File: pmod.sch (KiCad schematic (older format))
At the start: 13 parts, among them J6 PMOD, U10 AP7381-33SA, U11 TXS0108EPW

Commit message: finished routing, drc passed
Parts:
- U10: symbol Regulator_Linear:AP7381-33SA -> THS-80-rescue:AP7381-33SA-Regulator_Linear
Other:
- moved on the sheet: C14, C15
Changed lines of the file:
@@
 L power:VCC #PWR?
 U 1 1 5DC93B40
-P 2900 1875
+P 2850 2175
 AR Path="/5D70CA34/5DC93B40" Ref="#PWR?"  Part="1"
 AR Path="/5D70CA34/5DC790D1/5DC93B40" Ref="#PWR033"  Part="1"
-F 0 "#PWR033" H 2900 1725 50  0001 C CNN
-F 1 "VCC" H 2917 2048 50  0000 C CNN
-F 2 "" H 2900 1875 50  0001 C CNN
-F 3 "" H 2900 1875 50  0001 C CNN
-	1    2900 1875
+F 0 "#PWR033" H 2850 2025 50  0001 C CNN
+F 1 "VCC" H 2867 2348 50  0000 C CNN
+F 2 "" H 2850 2175 50  0001 C CNN
+F 3 "" H 2850 2175 50  0001 C CNN
+	1    2850 2175
 	1    0    0    -1
 $EndComp
@@
 L power:+3V3 #PWR?
 U 1 1 5DC93B46
-P 4350 1875
+P 4300 2175
 AR Path="/5D70CA34/5DC93B46" Ref="#PWR?"  Part="1"
 AR Path="/5D70CA34/5DC790D1/5DC93B46" Ref="#PWR077"  Part="1"
-F 0 "#PWR077" H 4350 1725 50  0001 C CNN
-F 1 "+3V3" H 4365 2048 50  0000 C CNN
-F 2 "" H 4350 1875 50  0001 C CNN
-F 3 "" H 4350 1875 50  0001 C CNN
-	1    4350 1875
-	1    0    0    -1
-$EndComp
-Wire Wire Line
-	3075 1875 2900 1875
-Connection ~ 3075 1875
-Wire Wire Line
-	3075 1925 3075 1875
-Wire Wire Line
-	4025 1875 4350 1875
-Connection ~ 4025 1875
-Wire Wire Line
-	4025 1925 4025 1875
-Wire Wire Line
-	3900 1875 4025 1875
-Wire Wire Line
-	3300 1875 3075 1875
+F 0 "#PWR077" H 4300 2025 50  0001 C CNN
+F 1 "+3V3" H 4315 2348 50  0000 C CNN
+F 2 "" H 4300 2175 50  0001 C CNN
+F 3 "" H 4300 2175 50  0001 C CNN
+	1    4300 2175
+	1    0    0    -1
+$EndComp
+Wire Wire Line
+	3025 2175 2850 2175
+Connection ~ 3025 2175
+Wire Wire Line
+	3025 2225 3025 2175
+Wire Wire Line
+	3975 2175 4300 2175
+Connection ~ 3975 2175
+Wire Wire Line
+	3975 2225 3975 2175
+Wire Wire Line
+	3850 2175 3975 2175
+Wire Wire Line
+	3250 2175 3025 2175
 $Comp
 L power:GND #PWR?
 U 1 1 5DC93B54
-P 3600 2175
+P 3550 2475
 AR Path="/5D70CA34/5DC93B54" Ref="#PWR?"  Part="1"
 AR Path="/5D70CA34/5DC790D1/5DC93B54" Ref="#PWR036"  Part="1"
-F 0 "#PWR036" H 3600 1925 50  0001 C CNN
-F 1 "GND" H 3605 2002 50  0000 C CNN
-F 2 "" H 3600 2175 50  0001 C CNN
-F 3 "" H 3600 2175 50  0001 C CNN
-	1    3600 2175
+F 0 "#PWR036" H 3550 2225 50  0001 C CNN
+F 1 "GND" H 3555 2302 50  0000 C CNN
+F 2 "" H 3550 2475 50  0001 C CNN
+F 3 "" H 3550 2475 50  0001 C CNN
+	1    3550 2475
 	1    0    0    -1
 $EndComp
@@
 L power:GND #PWR?
 U 1 1 5DC93B5A
-P 3075 2175
+P 3025 2475
 AR Path="/5D70CA34/5DC93B5A" Ref="#PWR?"  Part="1"
 AR Path="/5D70CA34/5DC790D1/5DC93B5A" Ref="#PWR034"  Part="1"
-F 0 "#PWR034" H 3075 1925 50  0001 C CNN
-F 1 "GND" H 3080 2002 50  0000 C CNN
-F 2 "" H 3075 2175 50  0001 C CNN
-F 3 "" H 3075 2175 50  0001 C CNN
-	1    3075 2175
-	1    0    0    -1
-$EndComp
-Wire Wire Line
-	3075 2125 3075 2175
+F 0 "#PWR034" H 3025 2225 50  0001 C CNN
+F 1 "GND" H 3030 2302 50  0000 C CNN
+F 2 "" H 3025 2475 50  0001 C CNN
+F 3 "" H 3025 2475 50  0001 C CNN
+	1    3025 2475
+	1    0    0    -1
+$EndComp
+Wire Wire Line
+	3025 2425 3025 2475
 $Comp
 L Device:C_Small C?
 U 1 1 5DC93B61
-P 3075 2025
+P 3025 2325
 AR Path="/5D70CA34/5DC93B61" Ref="C?"  Part="1"
 AR Path="/5D70CA34/5DC790D1/5DC93B61" Ref="C14"  Part="1"
-F 0 "C14" H 3167 2071 50  0000 L CNN
-F 1 "1uF" H 3167 1980 50  0000 L CNN
-F 2 "Capacitor_SMD:C_0603_1608Metric_Pad1.05x0.95mm_HandSolder" H 3075 2025 50  0001 C CNN
-F 3 "~" H 3075 2025 50  0001 C CNN
-	1    3075 2025
+F 0 "C14" H 3117 2371 50  0000 L CNN
+F 1 "1uF" H 3117 2280 50  0000 L CNN
+F 2 "Capacitor_SMD:C_0603_1608Metric_Pad1.05x0.95mm_HandSolder" H 3025 2325 50  0001 C CNN
+F 3 "~" H 3025 2325 50  0001 C CNN
+	1    3025 2325
 	1    0    0    -1
 $EndComp
@@
 L power:GND #PWR?
 U 1 1 5DC93B67
-P 4025 2175
+P 3975 2475
 AR Path="/5D70CA34/5DC93B67" Ref="#PWR?"  Part="1"
 AR Path="/5D70CA34/5DC790D1/5DC93B67" Ref="#PWR038"  Part="1"
-F 0 "#PWR038" H 4025 1925 50  0001 C CNN
-F 1 "GND" H 4030 2002 50  0000 C CNN
-F 2 "" H 4025 2175 50  0001 C CNN
-F 3 "" H 4025 2175 50  0001 C CNN
-	1    4025 2175
-	1    0    0    -1
-$EndComp
-Wire Wire Line
-	4025 2125 4025 2175
+F 0 "#PWR038" H 3975 2225 50  0001 C CNN
+F 1 "GND" H 3980 2302 50  0000 C CNN
+F 2 "" H 3975 2475 50  0001 C CNN
+F 3 "" H 3975 2475 50  0001 C CNN
+	1    3975 2475
+	1    0    0    -1
+$EndComp
+Wire Wire Line
+	3975 2425 3975 2475
 $Comp
 L Device:C_Small C?
 U 1 1 5DC93B6E
-P 4025 2025
+P 3975 2325
 AR Path="/5D70CA34/5DC93B6E" Ref="C?"  Part="1"
 AR Path="/5D70CA34/5DC790D1/5DC93B6E" Ref="C15"  Part="1"
-F 0 "C15" H 4117 2071 50  0000 L CNN
-F 1 "2.2uF" H 4117 1980 50  0000 L CNN
-F 2 "Capacitor_SMD:C_0603_1608Metric_Pad1.05x0.95mm_HandSolder" H 4025 2025 50  0001 C CNN
-F 3 "~" H 4025 2025 50  0001 C CNN
-	1    4025 2025
-	1    0    0    -1
-$EndComp
-$Comp
-L Regulator_Linear:AP7381-33SA U?
+F 0 "C15" H 4067 2371 50  0000 L CNN
+F 1 "2.2uF" H 4067 2280 50  0000 L CNN
+F 2 "Capacitor_SMD:C_0603_1608Metric_Pad1.05x0.95mm_HandSolder" H 3975 2325 50  0001 C CNN
+F 3 "~" H 3975 2325 50  0001 C CNN
+	1    3975 2325
+	1    0    0    -1
+$EndComp
+$Comp
+L THS-80-rescue:AP7381-33SA-Regulator_Linear U?
 U 1 1 5DC93B74
-P 3600 1875
+P 3550 2175
 AR Path="/5D70CA34/5DC93B74" Ref="U?"  Part="1"
 AR Path="/5D70CA34/5DC790D1/5DC93B74" Ref="U10"  Part="1"
-F 0 "U10" H 3600 2117 50  0000 C CNN
-F 1 "AP7381-33SA" H 3600 2026 50  0000 C CNN
-F 2 "Package_TO_SOT_SMD:SOT-23" H 3600 2100 50  0001 C CIN
-F 3 "https://www.mouser.com/datasheet/2/115/AP7381-1220674.pdf" H 3600 1825 50  0001 C CNN
-	1    3600 1875
+AR Path="/5DC93B74" Ref="U10"  Part="1"
+F 0 "U10" H 3550 2417 50  0000 C CNN
+F 1 "AP7381-33SA" H 3550 2326 50  0000 C CNN
+F 2 "Package_TO_SOT_SMD:SOT-23" H 3550 2400 50  0001 C CIN
+F 3 "https://www.mouser.com/datasheet/2/115/AP7381-1220674.pdf" H 3550 2125 50  0001 C CNN
+	1    3550 2175
 	1    0    0    -1
 $EndComp
@@
 $EndComp
 Wire Wire Line
-	6250 4200 5850 4200
-Wire Wire Line
-	6250 4100 5850 4100
-Wire Wire Line
-	6250 4000 5850 4000
-Wire Wire Line
-	6250 3900 5850 3900
+	6250 3500 5850 3500
+Wire Wire Line
+	6250 3600 5850 3600
+Wire Wire Line
+	6250 3700 5850 3700
+Wire Wire Line
+	6250 3800 5850 3800
 Text Label 7950 3500 0    50   ~ 0
 PMOD7
@@
 Text HLabel 6350 2500 0    50   Input ~ 0
 OE1
-Text Label 6000 4200 0    50   ~ 0
+Text Label 6000 4100 0    50   ~ 0
 R4
-Text Label 6000 4100 0    50   ~ 0
+Text Label 6000 3900 0    50   ~ 0
 R5
-Text Label 6000 4000 0    50   ~ 0
+Text Label 6000 3800 0    50   ~ 0
 R6
-Text Label 6000 3900 0    50   ~ 0
+Text Label 6000 3600 0    50   ~ 0
 R7
 $Comp
@@
 Text Label 6000 3500 0    50   ~ 0
 R3
-Text Label 6000 3600 0    50   ~ 0
+Text Label 6000 3700 0    50   ~ 0
 R2
-Text Label 6000 3700 0    50   ~ 0
+Text Label 6000 4000 0    50   ~ 0
 R1
-Text Label 6000 3800 0    50   ~ 0
+Text Label 6000 4200 0    50   ~ 0
 R0
 Wire Wire Line
-	6250 3500 5850 3500
-Wire Wire Line
-	6250 3600 5850 3600
-Wire Wire Line
-	6250 3700 5850 3700
-Wire Wire Line
-	6250 3800 5850 3800
+	6250 4200 5850 4200
+Wire Wire Line
+	6250 4100 5850 4100
+Wire Wire Line
+	6250 4000 5850 4000
+Wire Wire Line
+	6250 3900 5850 3900
 $Comp
 L Device:C_Small C?

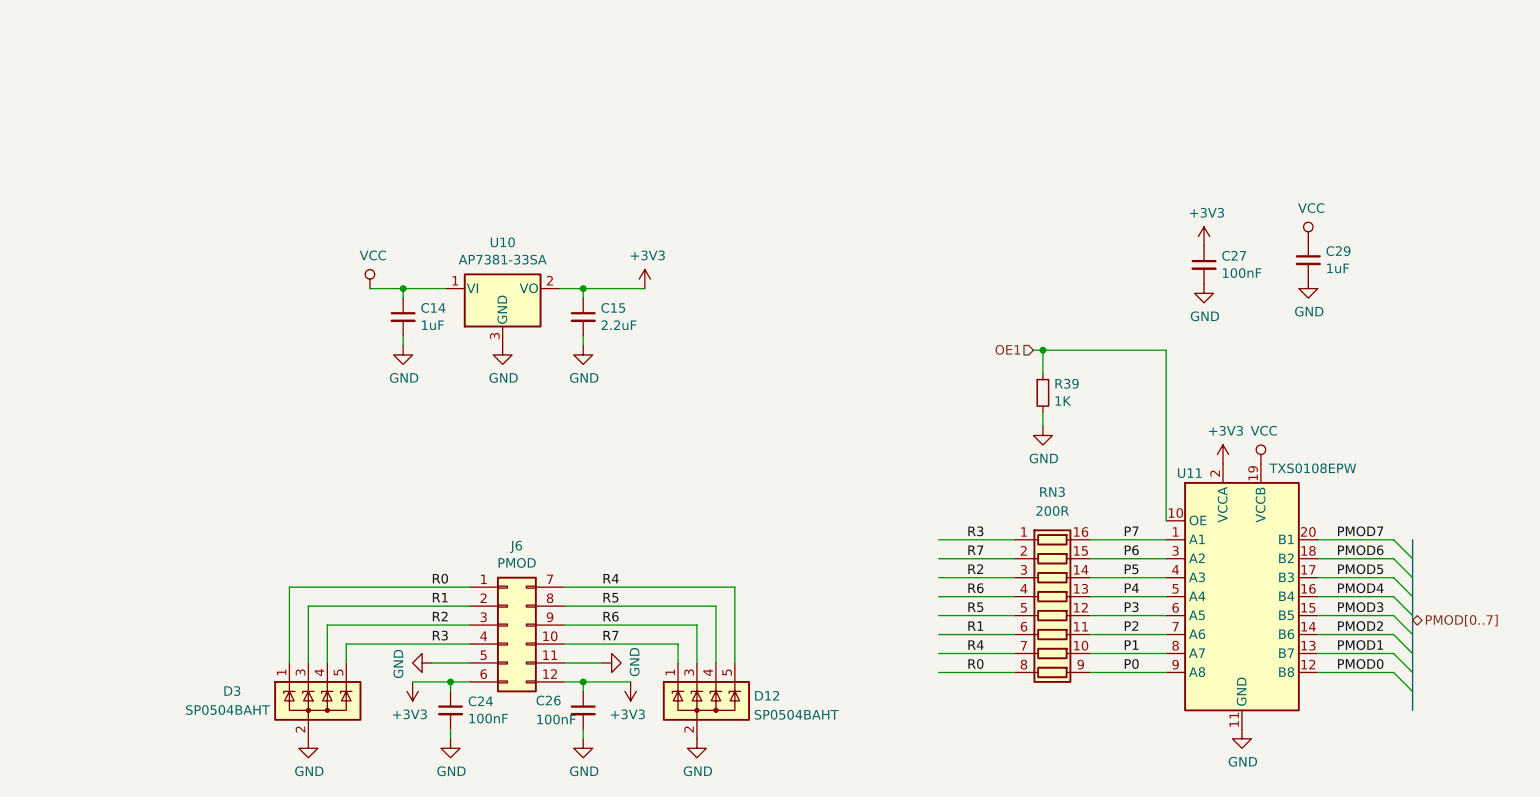
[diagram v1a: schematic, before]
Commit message: fixed pmod pins
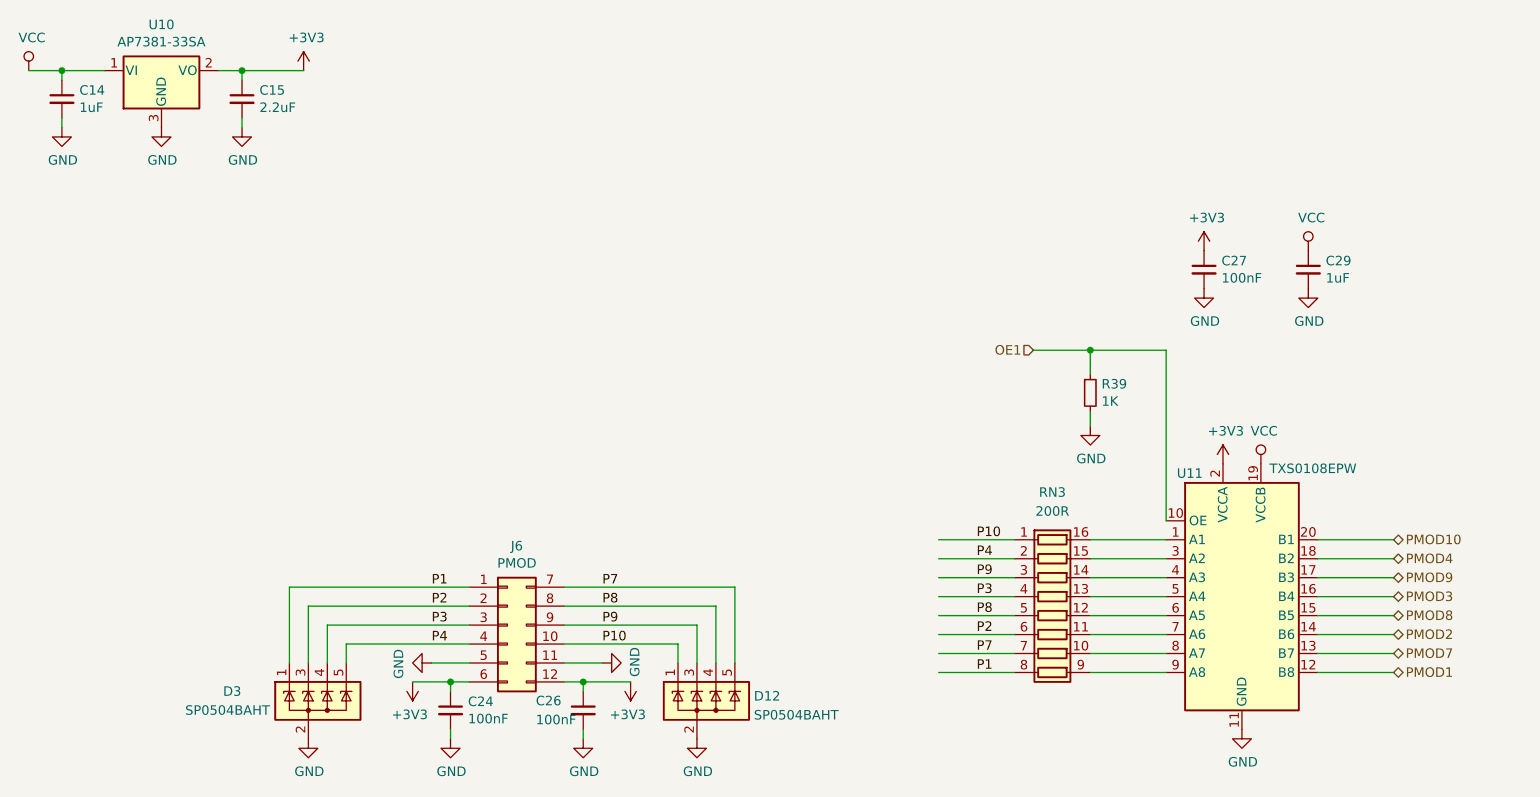
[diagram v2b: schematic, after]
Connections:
- net labels added: P10, P8, P9, PMOD10, PMOD8, PMOD9
- net labels removed: P0, P5, P6, PMOD0, PMOD5, PMOD6, PMOD[0..7], R0, R1, R2, R3, R4, R5, R6, R7
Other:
- moved on the sheet: C14, C15, C27, C29, R39, U10

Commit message: lots of fixes
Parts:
- C29: value 1uF -> 100nF
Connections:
- wire segments 63 -> 68
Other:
- moved on the sheet: C14, C15, C24, C26, C27, C29, D12, D3, J6, R39, RN3, U10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

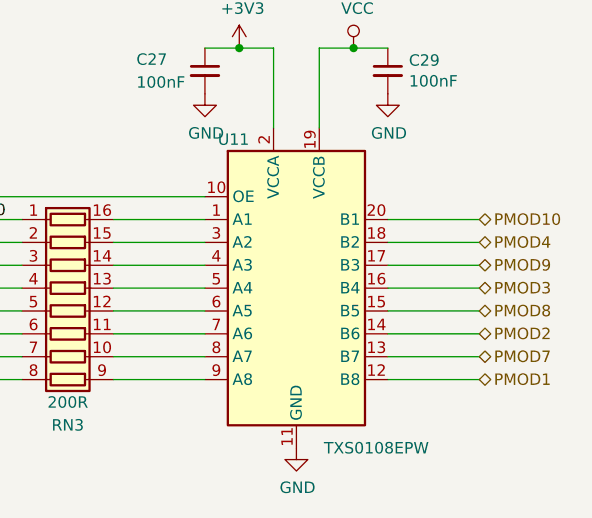
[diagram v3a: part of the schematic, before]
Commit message: fixed led values, added pwr led
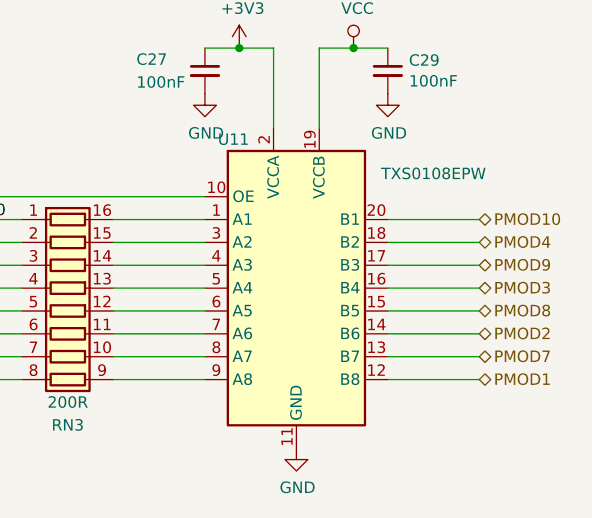
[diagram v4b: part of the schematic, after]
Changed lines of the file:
@@
 P 7150 3700
 F 0 "U11" H 6875 4350 50  0000 C CNN
-F 1 "TXS0108EPW" H 7500 3000 50  0000 C CNN
+F 1 "TXS0108EPW" H 7750 4200 50  0000 C CNN
 F 2 "Package_SO:TSSOP-20_4.4x6.5mm_P0.65mm" H 7150 2950 50  0001 C CNN
 F 3 "www.ti.com/lit/ds/symlink/txs0108e.pdf" H 7150 3600 50  0001 C CNN

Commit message: lots of fixes
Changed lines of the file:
@@
 U 1 1 5DF4B0EE
 P 7150 3700
-F 0 "U11" H 6875 4350 50  0000 C CNN
-F 1 "TXS0108EPW" H 7750 4200 50  0000 C CNN
+F 0 "U11" H 7150 3700 50  0000 C CNN
+F 1 "TXS0108EPW" H 7700 4200 50  0000 C CNN
 F 2 "Package_SO:TSSOP-20_4.4x6.5mm_P0.65mm" H 7150 2950 50  0001 C CNN
 F 3 "www.ti.com/lit/ds/symlink/txs0108e.pdf" H 7150 3600 50  0001 C CNN
